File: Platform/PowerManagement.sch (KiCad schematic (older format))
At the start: 29 parts, among them J1 12V INPUT, J2 12V_INPUT, J3 Barrel_Jack, U1 LM7805_TO220, U2 LM317_TO-220

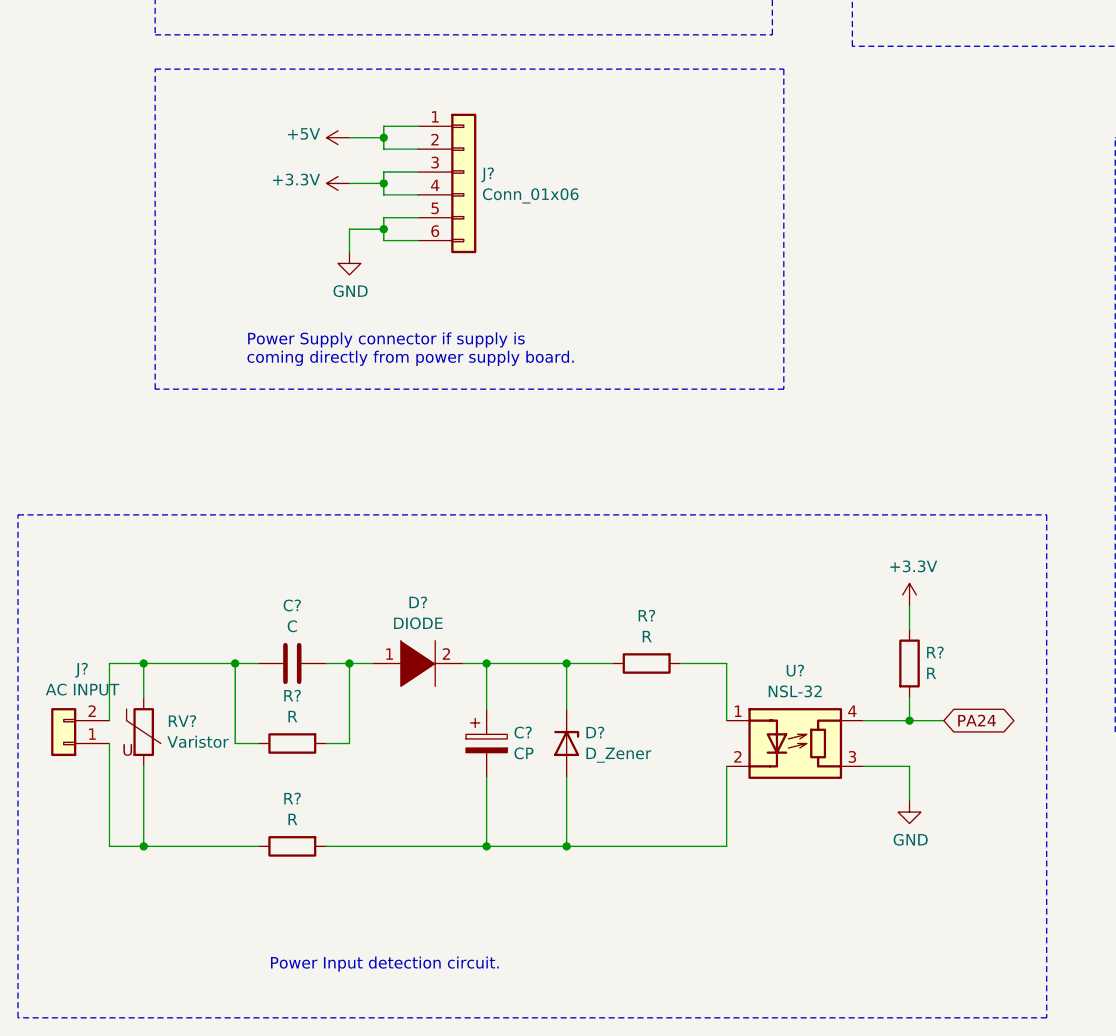
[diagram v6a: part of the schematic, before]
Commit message: Added power input detection circuit.
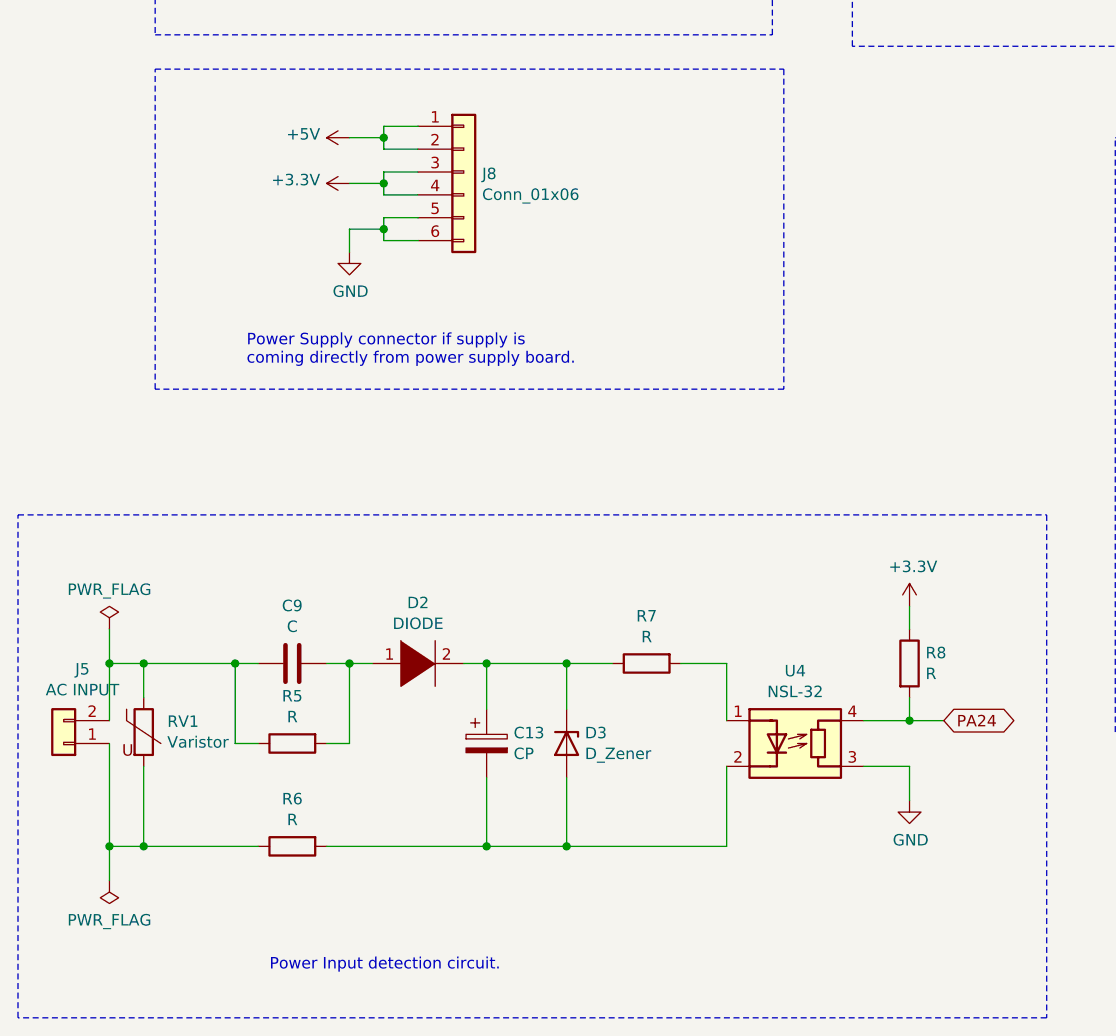
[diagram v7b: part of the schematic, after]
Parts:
- gave numbers to parts that had none: 12
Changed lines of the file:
@@
 	5150 2000 6000 2000
 $Comp
-L Connector_Generic:Conn_01x06 J?
+L Connector_Generic:Conn_01x06 J8
 U 1 1 60174FE6
 P 2650 3600
-F 0 "J?" H 2730 3592 50  0000 L CNN
+F 0 "J8" H 2730 3592 50  0000 L CNN
 F 1 "Conn_01x06" H 2730 3501 50  0000 L CNN
 F 2 "" H 2650 3600 50  0001 C CNN
@@
 	2300 3900 2450 3900
 $Comp
-L power:GND #PWR?
+L power:GND #PWR019
 U 1 1 60179FD7
 P 2150 3950
-F 0 "#PWR?" H 2150 3700 50  0001 C CNN
+F 0 "#PWR019" H 2150 3700 50  0001 C CNN
 F 1 "GND" H 2155 3777 50  0000 C CNN
 F 2 "" H 2150 3950 50  0001 C CNN
@@
 	2300 3850 2300 3900
 $Comp
-L power:+5V #PWR?
+L power:+5V #PWR017
 U 1 1 6017E3B0
 P 2150 3450
-F 0 "#PWR?" H 2150 3300 50  0001 C CNN
+F 0 "#PWR017" H 2150 3300 50  0001 C CNN
 F 1 "+5V" V 2165 3578 50  0000 L CNN
 F 2 "" H 2150 3450 50  0001 C CNN
@@
 	2300 3600 2300 3650
 $Comp
-L power:+3.3V #PWR?
+L power:+3.3V #PWR018
 U 1 1 6018128A
 P 2150 3650
-F 0 "#PWR?" H 2150 3500 50  0001 C CNN
+F 0 "#PWR018" H 2150 3500 50  0001 C CNN
 F 1 "+3.3V" V 2165 3778 50  0000 L CNN
 F 2 "" H 2150 3650 50  0001 C CNN
@@
 Power Supply connector if supply is\ncoming directly from power supply board.
 $Comp
-L Connector_Generic:Conn_01x02 J?
+L Connector_Generic:Conn_01x02 J5
 U 1 1 606CD559
 P 900 6100
-F 0 "J?" H 818 5775 50  0000 C CNN
+F 0 "J5" H 818 5775 50  0000 C CNN
 F 1 "AC INPUT" H 818 5866 50  0000 C CNN
 F 2 "" H 900 6100 50  0001 C CNN
@@
 $EndComp
 $Comp
-L Device:Varistor RV?
+L Device:Varistor RV1
 U 1 1 606CE1F7
 P 1250 6050
-F 0 "RV?" H 1353 6096 50  0000 L CNN
+F 0 "RV1" H 1353 6096 50  0000 L CNN
 F 1 "Varistor" H 1353 6005 50  0000 L CNN
 F 2 "" V 1180 6050 50  0001 C CNN
@@
 $EndComp
 $Comp
-L Device:C C?
+L Device:C C9
 U 1 1 606CE509
 P 1900 5750
-F 0 "C?" V 2152 5750 50  0000 C CNN
+F 0 "C9" V 2152 5750 50  0000 C CNN
 F 1 "C" V 2061 5750 50  0000 C CNN
 F 2 "" H 1938 5600 50  0001 C CNN
@@
 $EndComp
 $Comp
-L Device:R R?
+L Device:R R5
 U 1 1 606CEB7C
 P 1900 6100
-F 0 "R?" V 1693 6100 50  0000 C CNN
+F 0 "R5" V 1693 6100 50  0000 C CNN
 F 1 "R" V 1784 6100 50  0000 C CNN
 F 2 "" V 1830 6100 50  0001 C CNN
@@
 $EndComp
 $Comp
-L Device:R R?
+L Device:R R6
 U 1 1 606CFDC9
 P 1900 6550
-F 0 "R?" V 1693 6550 50  0000 C CNN
+F 0 "R6" V 1693 6550 50  0000 C CNN
 F 1 "R" V 1784 6550 50  0000 C CNN
 F 2 "" V 1830 6550 50  0001 C CNN
@@
 $EndComp
 $Comp
-L pspice:DIODE D?
+L pspice:DIODE D2
 U 1 1 606D01FE
 P 2450 5750
-F 0 "D?" H 2450 6015 50  0000 C CNN
+F 0 "D2" H 2450 6015 50  0000 C CNN
 F 1 "DIODE" H 2450 5924 50  0000 C CNN
 F 2 "" H 2450 5750 50  0001 C CNN
@@
 $EndComp
 $Comp
-L Device:CP C?
+L Device:CP C13
 U 1 1 606D06CF
 P 2750 6100
-F 0 "C?" H 2868 6146 50  0000 L CNN
+F 0 "C13" H 2868 6146 50  0000 L CNN
 F 1 "CP" H 2868 6055 50  0000 L CNN
 F 2 "" H 2788 5950 50  0001 C CNN
@@
 $EndComp
 $Comp
-L Device:D_Zener D?
+L Device:D_Zener D3
 U 1 1 606D11AD
 P 3100 6100
-F 0 "D?" V 3054 6180 50  0000 L CNN
+F 0 "D3" V 3054 6180 50  0000 L CNN
 F 1 "D_Zener" V 3145 6180 50  0000 L CNN
 F 2 "" H 3100 6100 50  0001 C CNN
@@
 $EndComp
 $Comp
-L Device:R R?
+L Device:R R7
 U 1 1 606D1903
 P 3450 5750
-F 0 "R?" V 3243 5750 50  0000 C CNN
+F 0 "R7" V 3243 5750 50  0000 C CNN
 F 1 "R" V 3334 5750 50  0000 C CNN
 F 2 "" V 3380 5750 50  0001 C CNN
@@
 $EndComp
 $Comp
-L Isolator:NSL-32 U?
+L Isolator:NSL-32 U4
 U 1 1 606D3219
 P 4100 6100
-F 0 "U?" H 4100 6417 50  0000 C CNN
+F 0 "U4" H 4100 6417 50  0000 C CNN
 F 1 "NSL-32" H 4100 6326 50  0000 C CNN
 F 2 "OptoDevice:Luna_NSL-32" H 4100 5800 50  0001 C CNN
@@
 	3100 5750 3300 5750
 $Comp
-L Device:R R?
+L Device:R R8
 U 1 1 606FCAB5
 P 4600 5750
-F 0 "R?" H 4670 5796 50  0000 L CNN
+F 0 "R8" H 4670 5796 50  0000 L CNN
 F 1 "R" H 4670 5705 50  0000 L CNN
 F 2 "" V 4530 5750 50  0001 C CNN
@@
 	4600 6000 4600 5900
 $Comp
-L power:GND #PWR?
+L power:GND #PWR025
 U 1 1 607009D1
 P 4600 6350
-F 0 "#PWR?" H 4600 6100 50  0001 C CNN
+F 0 "#PWR025" H 4600 6100 50  0001 C CNN
 F 1 "GND" H 4605 6177 50  0000 C CNN
 F 2 "" H 4600 6350 50  0001 C CNN
@@
 	4600 6200 4400 6200
 $Comp
-L power:+3.3V #PWR?
+L power:+3.3V #PWR023
 U 1 1 6070548F
 P 4600 5500
-F 0 "#PWR?" H 4600 5350 50  0001 C CNN
+F 0 "#PWR023" H 4600 5350 50  0001 C CNN
 F 1 "+3.3V" H 4615 5673 50  0000 C CNN
 F 2 "" H 4600 5500 50  0001 C CNN
@@
 Text Notes 1800 7100 0    50   ~ 0
 Power Input detection circuit.
+$Comp
+L power:PWR_FLAG #FLG0101
+U 1 1 6067C06F
+P 1100 5600
+F 0 "#FLG0101" H 1100 5675 50  0001 C CNN
+F 1 "PWR_FLAG" H 1100 5773 50  0000 C CNN
+F 2 "" H 1100 5600 50  0001 C CNN
+F 3 "~" H 1100 5600 50  0001 C CNN
+	1    1100 5600
+	1    0    0    -1
+$EndComp
+$Comp
+L power:PWR_FLAG #FLG0102
+U 1 1 6067C371
+P 1100 6700
+F 0 "#FLG0102" H 1100 6775 50  0001 C CNN
+F 1 "PWR_FLAG" H 1100 6873 50  0000 C CNN
+F 2 "" H 1100 6700 50  0001 C CNN
+F 3 "~" H 1100 6700 50  0001 C CNN
+	1    1100 6700
+	-1   0    0    1
+$EndComp
+Wire Wire Line
+	1100 5600 1100 5750
+Connection ~ 1100 5750
+Wire Wire Line
+	1100 6550 1100 6700
+Connection ~ 1100 6550
 $EndSCHEMATC

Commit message: Added connector for relay controls.
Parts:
- D2: footprint (none) -> Diode_THT:D_DO-41_SOD81_P10.16mm_Horizontal
- R1, R2, R5, R6, R7, R8: footprint (none) -> Resistor_SMD:R_0603_1608Metric
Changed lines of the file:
@@
 F 0 "R1" H 7920 4696 50  0000 L CNN
 F 1 "1K" H 7920 4605 50  0000 L CNN
-F 2 "" V 7780 4650 50  0001 C CNN
+F 2 "Resistor_SMD:R_0603_1608Metric" V 7780 4650 50  0001 C CNN
 F 3 "~" H 7850 4650 50  0001 C CNN
 	1    7850 4650
@@
 F 0 "R2" H 7920 5296 50  0000 L CNN
 F 1 "5.1K" H 7920 5205 50  0000 L CNN
-F 2 "" V 7780 5250 50  0001 C CNN
+F 2 "Resistor_SMD:R_0603_1608Metric" V 7780 5250 50  0001 C CNN
 F 3 "~" H 7850 5250 50  0001 C CNN
 	1    7850 5250
@@
 F 0 "R5" V 1693 6100 50  0000 C CNN
 F 1 "R" V 1784 6100 50  0000 C CNN
-F 2 "" V 1830 6100 50  0001 C CNN
+F 2 "Resistor_SMD:R_0603_1608Metric" V 1830 6100 50  0001 C CNN
 F 3 "~" H 1900 6100 50  0001 C CNN
 	1    1900 6100
@@
 F 0 "R6" V 1693 6550 50  0000 C CNN
 F 1 "R" V 1784 6550 50  0000 C CNN
-F 2 "" V 1830 6550 50  0001 C CNN
+F 2 "Resistor_SMD:R_0603_1608Metric" V 1830 6550 50  0001 C CNN
 F 3 "~" H 1900 6550 50  0001 C CNN
 	1    1900 6550
@@
 F 0 "D2" H 2450 6015 50  0000 C CNN
 F 1 "DIODE" H 2450 5924 50  0000 C CNN
-F 2 "" H 2450 5750 50  0001 C CNN
+F 2 "Diode_THT:D_DO-41_SOD81_P10.16mm_Horizontal" H 2450 5750 50  0001 C CNN
 F 3 "~" H 2450 5750 50  0001 C CNN
 	1    2450 5750
@@
 F 0 "R7" V 3243 5750 50  0000 C CNN
 F 1 "R" V 3334 5750 50  0000 C CNN
-F 2 "" V 3380 5750 50  0001 C CNN
+F 2 "Resistor_SMD:R_0603_1608Metric" V 3380 5750 50  0001 C CNN
 F 3 "~" H 3450 5750 50  0001 C CNN
 	1    3450 5750
@@
 F 0 "R8" H 4670 5796 50  0000 L CNN
 F 1 "R" H 4670 5705 50  0000 L CNN
-F 2 "" V 4530 5750 50  0001 C CNN
+F 2 "Resistor_SMD:R_0603_1608Metric" V 4530 5750 50  0001 C CNN
 F 3 "~" H 4600 5750 50  0001 C CNN
 	1    4600 5750
